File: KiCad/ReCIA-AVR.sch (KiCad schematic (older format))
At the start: 6 parts, among them U1 AVR128DA64-I_MR, U5 8520_DIP

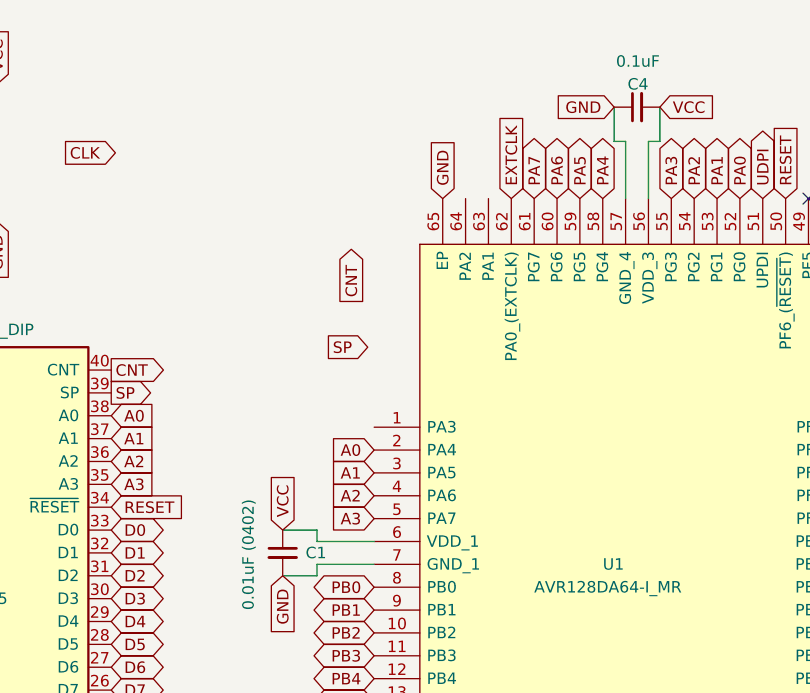
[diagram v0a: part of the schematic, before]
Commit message: Pin assignment of A0-A3, SP, CNT signals for the AVR-version and more routing done
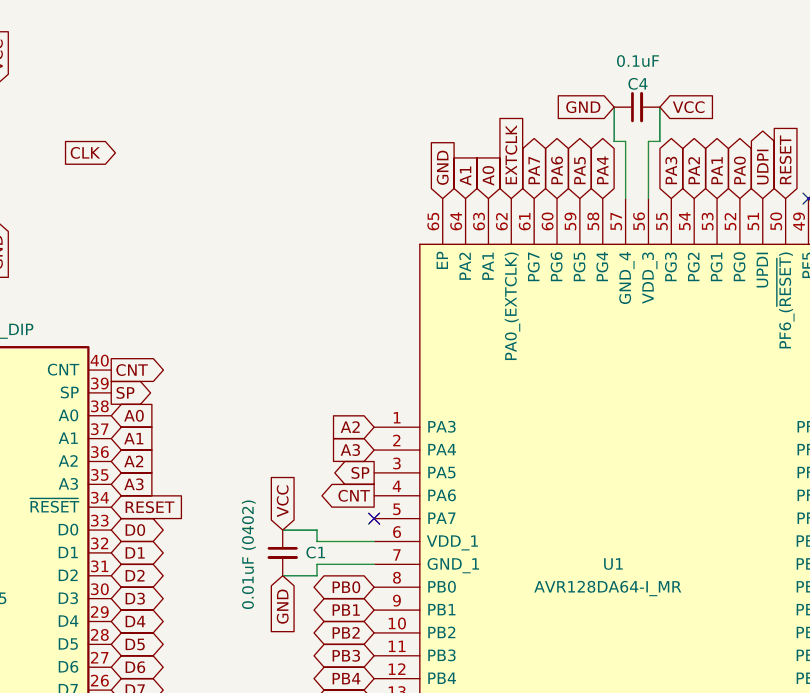
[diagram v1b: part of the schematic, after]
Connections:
- no-connect marks 13 -> 14
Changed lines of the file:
@@
 Text GLabel 5100 1650 1    50   BiDi ~ 0
 PA7
+Text GLabel 4900 1650 1    50   Input ~ 0
+A0
+Text GLabel 4800 1650 1    50   Input ~ 0
+A1
+Text GLabel 4400 2650 0    50   Input ~ 0
+A2
 Text GLabel 4400 2750 0    50   Input ~ 0
-A0
-Text GLabel 4400 2850 0    50   Input ~ 0
-A1
-Text GLabel 4400 2950 0    50   Input ~ 0
-A2
-Text GLabel 4400 3050 0    50   Input ~ 0
 A3
 Text GLabel 6100 1650 1    50   BiDi ~ 0
@@
 Text GLabel 5000 1650 1    50   Input ~ 0
 EXTCLK
-Text GLabel 4300 2100 1    50   Output ~ 0
+Text GLabel 4400 2950 0    50   Output ~ 0
 CNT
-Text GLabel 4200 2300 2    50   Output ~ 0
+Text GLabel 4400 2850 0    50   Output ~ 0
 SP
 NoConn ~ 6600 3150
@@
 Wire Wire Line
 	5150 5100 5150 5250
+NoConn ~ 4400 3050
 $EndSCHEMATC

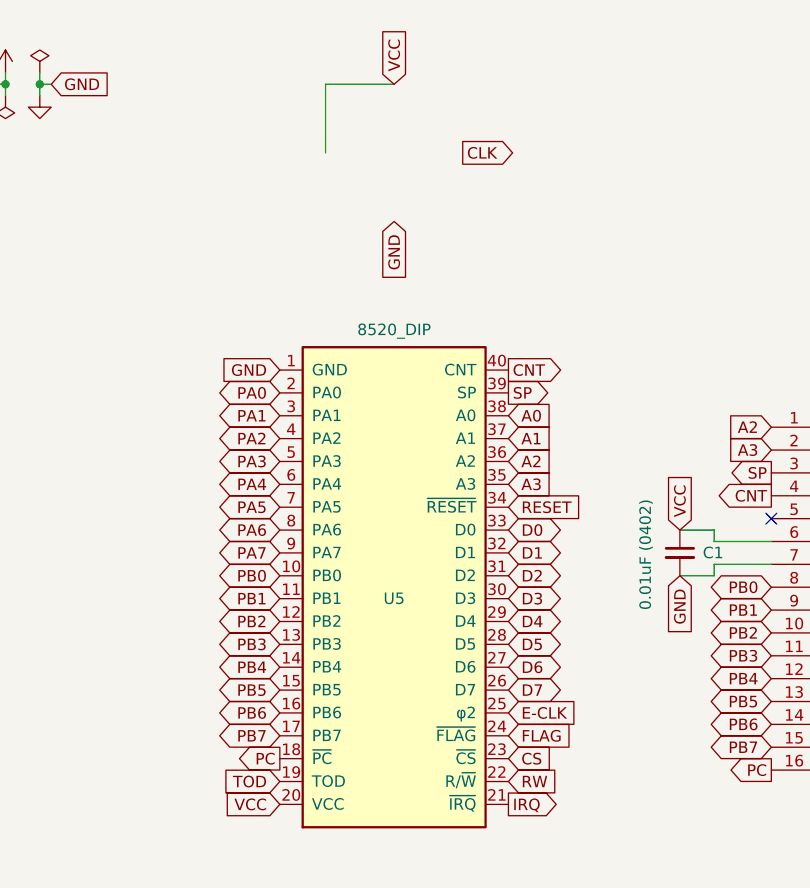
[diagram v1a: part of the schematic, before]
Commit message: Add a 74AHCT1G17 - Single Schmitt trigger buffer for the E-CLK on the AVR version
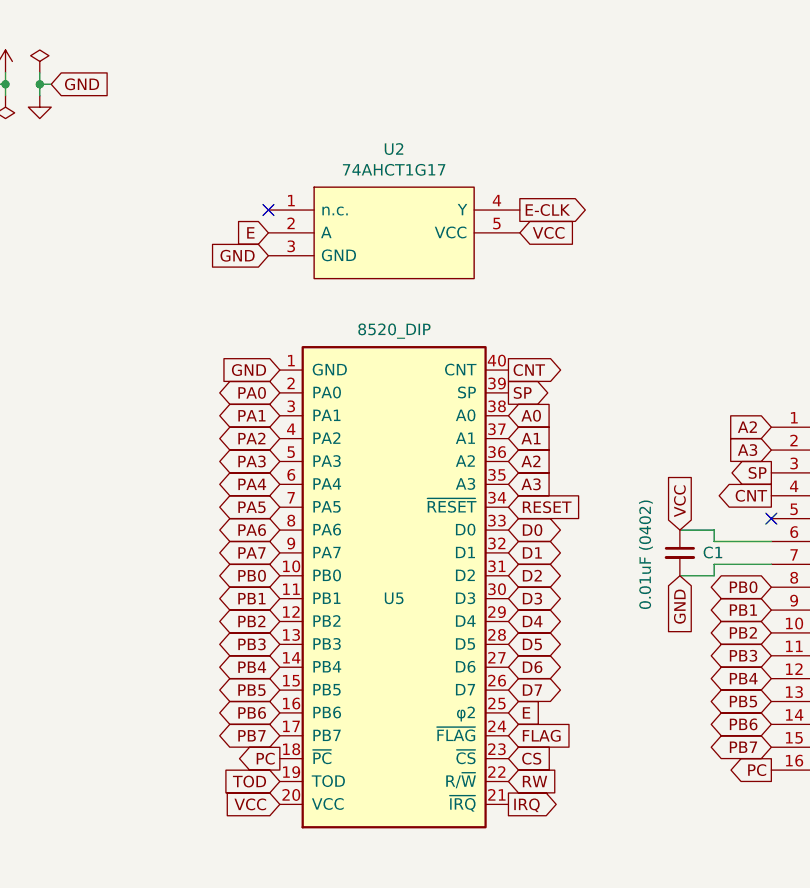
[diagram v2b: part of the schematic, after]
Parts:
- added U2: 74AHCT1G17, ReCIA:SOT95P275X110-5N, symbol ReCIA:74AHCT1G17
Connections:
- net labels added: E
- net labels removed: CLK
- wire segments 32 -> 30
- no-connect marks 14 -> 15
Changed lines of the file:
@@
 Text GLabel 3250 3800 2    50   BiDi ~ 0
 D7
-Text GLabel 3250 3900 2    50   Input ~ 0
+Text GLabel 3300 1700 2    50   Output ~ 0
 E-CLK
 Text GLabel 2250 4100 0    50   Output ~ 0
@@
 NoConn ~ 6600 2650
 NoConn ~ 6300 1650
-Text GLabel 2750 1750 3    50   Input ~ 0
-GND
-Text GLabel 2750 1150 1    50   Input ~ 0
-VCC
-Wire Wire Line
-	2450 1450 2450 1150
-Wire Wire Line
-	2450 1150 2750 1150
-Text GLabel 3050 1450 2    50   Output ~ 0
-CLK
 $Comp
 L Device:C_Small C1
@@
 	5150 5100 5150 5250
 NoConn ~ 4400 3050
+$Comp
+L ReCIA:74AHCT1G17 U2
+U 1 1 677A8B23
+P 2750 1800
+F 0 "U2" H 2750 2165 50  0000 C CNN
+F 1 "74AHCT1G17" H 2750 2074 50  0000 C CNN
+F 2 "ReCIA:SOT95P275X110-5N" H 3150 2000 50  0001 L CNN
+F 3 "https://assets.nexperia.com/documents/data-sheet/74AHC_AHCT1G17.pdf" H 3150 1900 50  0001 L CNN
+	1    2750 1800
+	1    0    0    -1
+$EndComp
+Text GLabel 2200 1900 0    50   Input ~ 0
+GND
+NoConn ~ 2200 1700
+Text GLabel 3300 1800 2    50   Input ~ 0
+VCC
+Text GLabel 3250 3900 2    50   Input ~ 0
+E
+Text GLabel 2200 1800 0    50   Input ~ 0
+E
 $EndSCHEMATC

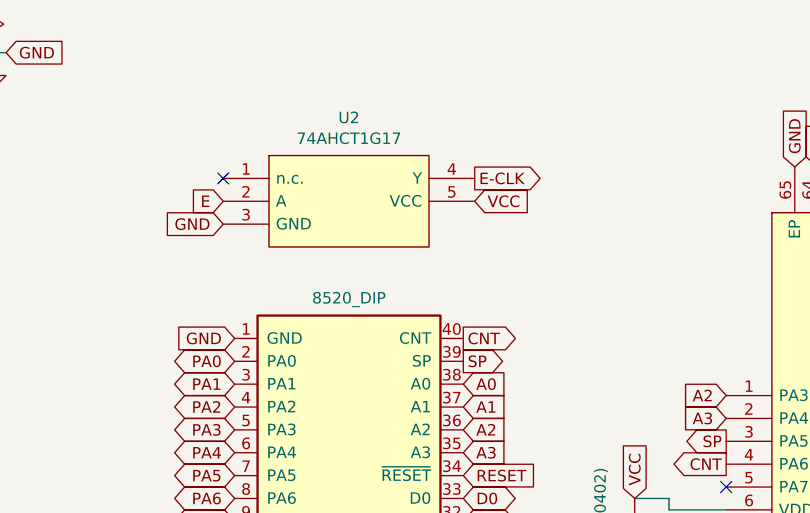
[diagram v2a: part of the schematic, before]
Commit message: Add decoupling cap for 74AHCT1G17 on the AVR version
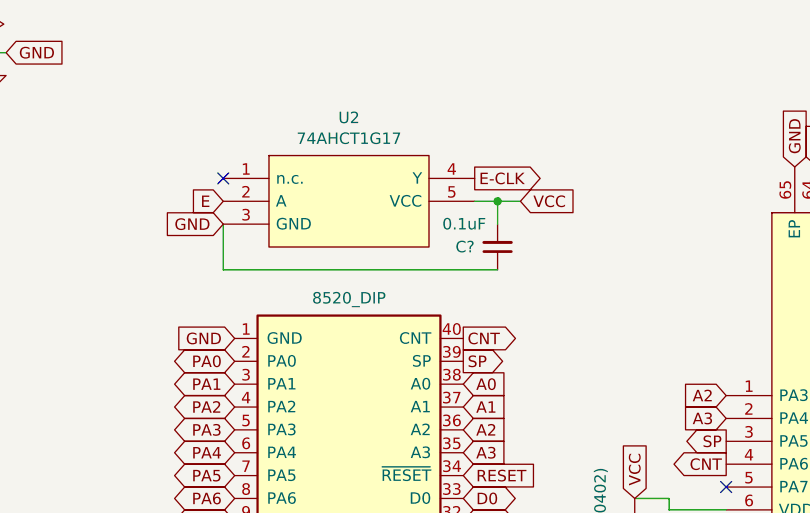
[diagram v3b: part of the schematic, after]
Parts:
- added C?: 0.1uF, Capacitor_SMD:C_0603_1608Metric_Pad1.08x0.95mm_HandSolder, symbol Device:C_Small
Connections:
- net GND: now also C?.1
- net VCC: now also C?.2
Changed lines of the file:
@@
 GND
 NoConn ~ 2200 1700
-Text GLabel 3300 1800 2    50   Input ~ 0
+Text GLabel 3500 1800 2    50   Input ~ 0
 VCC
 Text GLabel 3250 3900 2    50   Input ~ 0
@@
 Text GLabel 2200 1800 0    50   Input ~ 0
 E
+$Comp
+L Device:C_Small C?
+U 1 1 677B6FA1
+P 3400 2000
+F 0 "C?" H 3500 2000 50  0000 L CNN
+F 1 "0.1uF" H 3450 1900 50  0000 L CNN
+F 2 "Capacitor_SMD:C_0603_1608Metric_Pad1.08x0.95mm_HandSolder" H 3400 2000 50  0001 C CNN
+F 3 "~" H 3400 2000 50  0001 C CNN
+	1    3400 2000
+	-1   0    0    1
+$EndComp
+Wire Wire Line
+	3300 1800 3400 1800
+Wire Wire Line
+	3400 1900 3400 1800
+Connection ~ 3400 1800
+Wire Wire Line
+	3400 1800 3500 1800
+Wire Wire Line
+	3400 2100 2200 2100
+Wire Wire Line
+	2200 2100 2200 1900
 $EndSCHEMATC

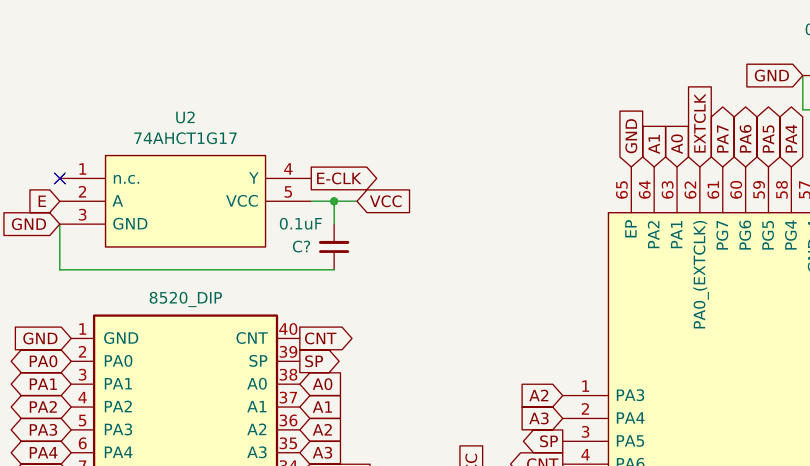
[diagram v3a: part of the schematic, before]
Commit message: Add a 33 Ohm damping resistor on the E-CLK buffer out line
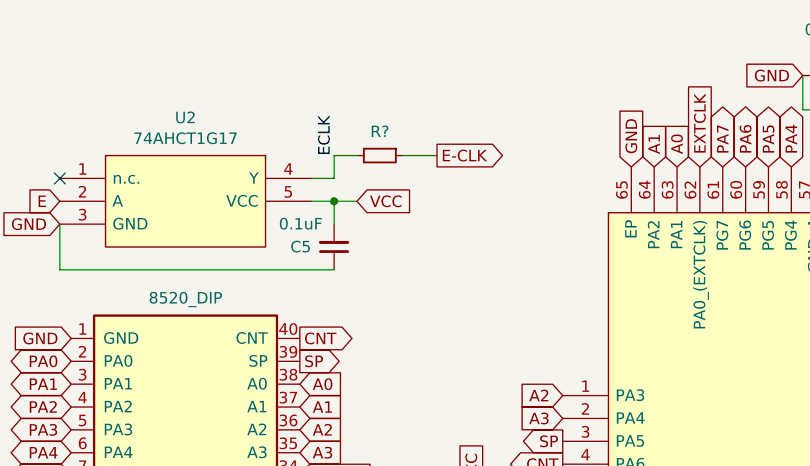
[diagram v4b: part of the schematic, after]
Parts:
- added R?: 33, Resistor_SMD:R_0603_1608Metric_Pad0.98x0.95mm_HandSolder, symbol Device:R_Small
- gave numbers to parts that had none: 1
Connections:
- net E-CLK: now also R?.1; no longer U2.4 (Y)
- new net ECLK: R?.2, U2.4 (Y)
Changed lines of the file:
@@
 Text GLabel 3250 3800 2    50   BiDi ~ 0
 D7
-Text GLabel 3300 1700 2    50   Output ~ 0
+Text GLabel 3850 1600 2    50   Output ~ 0
 E-CLK
 Text GLabel 2250 4100 0    50   Output ~ 0
@@
 E
 $Comp
-L Device:C_Small C?
+L Device:C_Small C5
 U 1 1 677B6FA1
 P 3400 2000
-F 0 "C?" H 3500 2000 50  0000 L CNN
+F 0 "C5" H 3500 2000 50  0000 L CNN
 F 1 "0.1uF" H 3450 1900 50  0000 L CNN
 F 2 "Capacitor_SMD:C_0603_1608Metric_Pad1.08x0.95mm_HandSolder" H 3400 2000 50  0001 C CNN
@@
 Wire Wire Line
 	2200 2100 2200 1900
+$Comp
+L Device:R_Small R?
+U 1 1 677C3D65
+P 3600 1600
+F 0 "R?" V 3496 1600 50  0000 C CNN
+F 1 "33" V 3495 1600 50  0001 C CNN
+F 2 "Resistor_SMD:R_0603_1608Metric_Pad0.98x0.95mm_HandSolder" H 3600 1600 50  0001 C CNN
+F 3 "~" H 3600 1600 50  0001 C CNN
+	1    3600 1600
+	0    1    1    0
+$EndComp
+Wire Wire Line
+	3300 1700 3400 1700
+Wire Wire Line
+	3400 1700 3400 1600
+Wire Wire Line
+	3400 1600 3500 1600
+Wire Wire Line
+	3700 1600 3850 1600
+Text Label 3400 1600 1    50   ~ 0
+ECLK
 $EndSCHEMATC

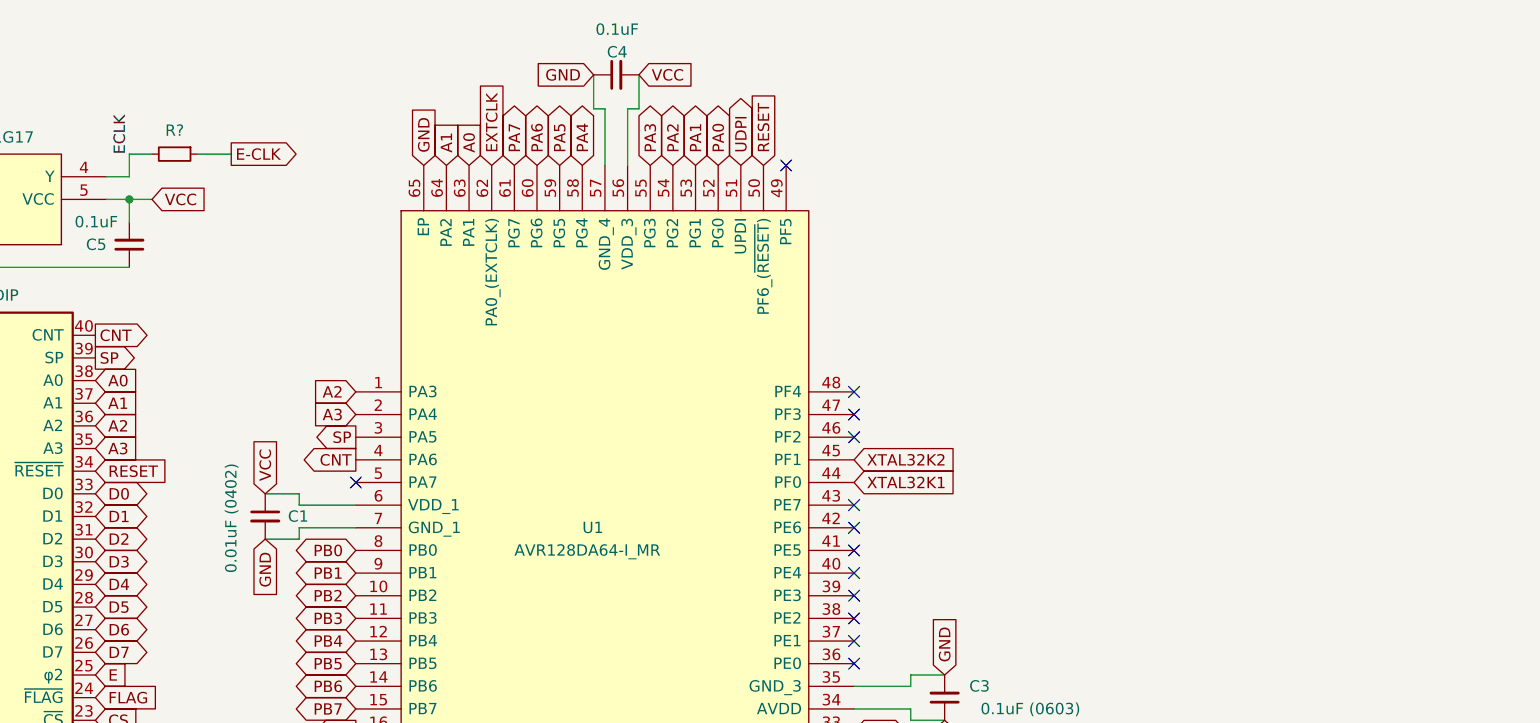
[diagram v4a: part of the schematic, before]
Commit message: Add TLC2932AIPWR to the AVR version
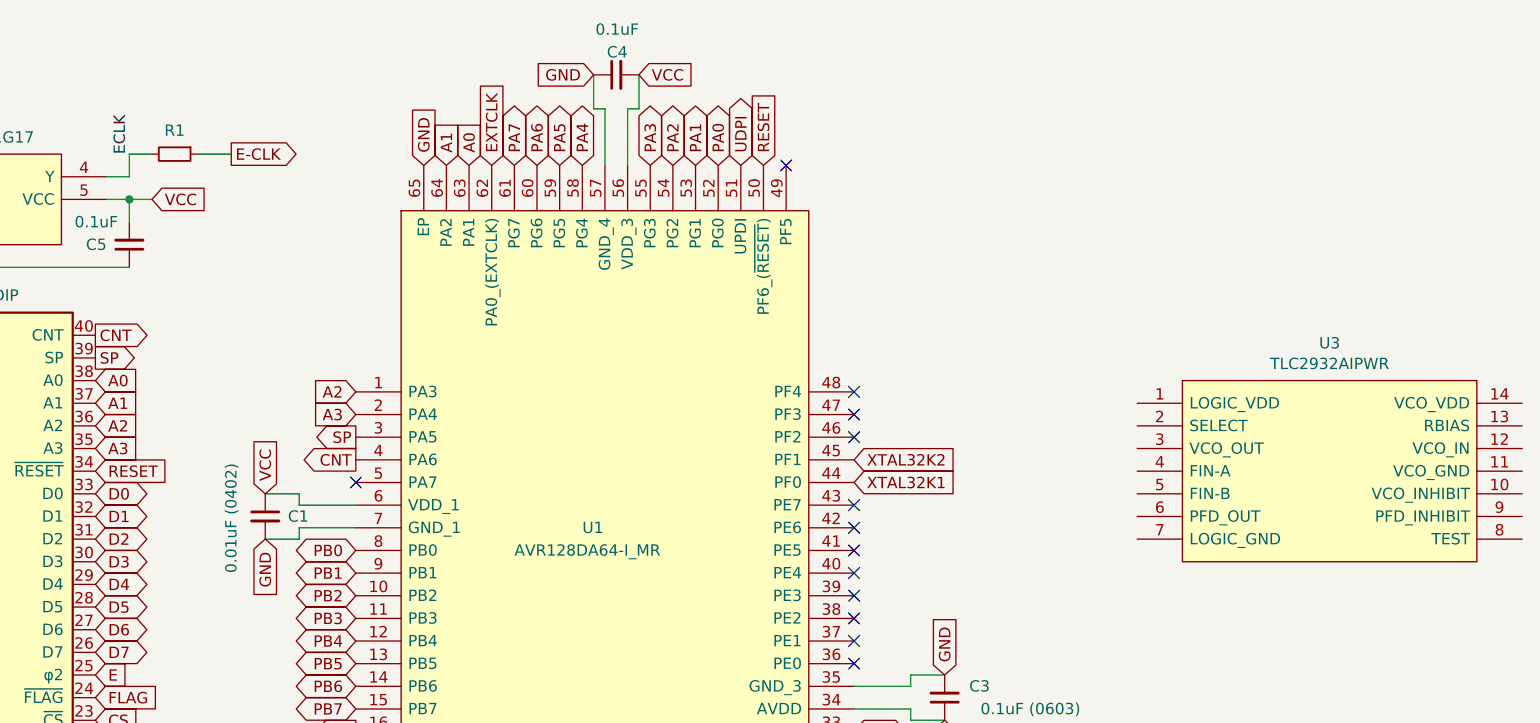
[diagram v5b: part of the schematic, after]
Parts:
- added U3: TLC2932AIPWR, Package_SO:TSSOP-14_4.4x5mm_P0.65mm, symbol ReCIA:TLC2932AIPWR
- gave numbers to parts that had none: 1
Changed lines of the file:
@@
 	2200 2100 2200 1900
 $Comp
-L Device:R_Small R?
+L Device:R_Small R1
 U 1 1 677C3D65
 P 3600 1600
-F 0 "R?" V 3496 1600 50  0000 C CNN
+F 0 "R1" V 3496 1600 50  0000 C CNN
 F 1 "33" V 3495 1600 50  0001 C CNN
 F 2 "Resistor_SMD:R_0603_1608Metric_Pad0.98x0.95mm_HandSolder" H 3600 1600 50  0001 C CNN
@@
 Text Label 3400 1600 1    50   ~ 0
 ECLK
+$Comp
+L ReCIA:TLC2932AIPWR U3
+U 1 1 677DB716
+P 8650 2950
+F 0 "U3" H 8700 3465 50  0000 C CNN
+F 1 "TLC2932AIPWR" H 8700 3374 50  0000 C CNN
+F 2 "Package_SO:TSSOP-14_4.4x5mm_P0.65mm" H 9400 3300 50  0001 L CNN
+F 3 "http://www.ti.com/lit/gpn/TLC2932A" H 9400 3200 50  0001 L CNN
+	1    8650 2950
+	1    0    0    -1
+$EndComp
 $EndSCHEMATC

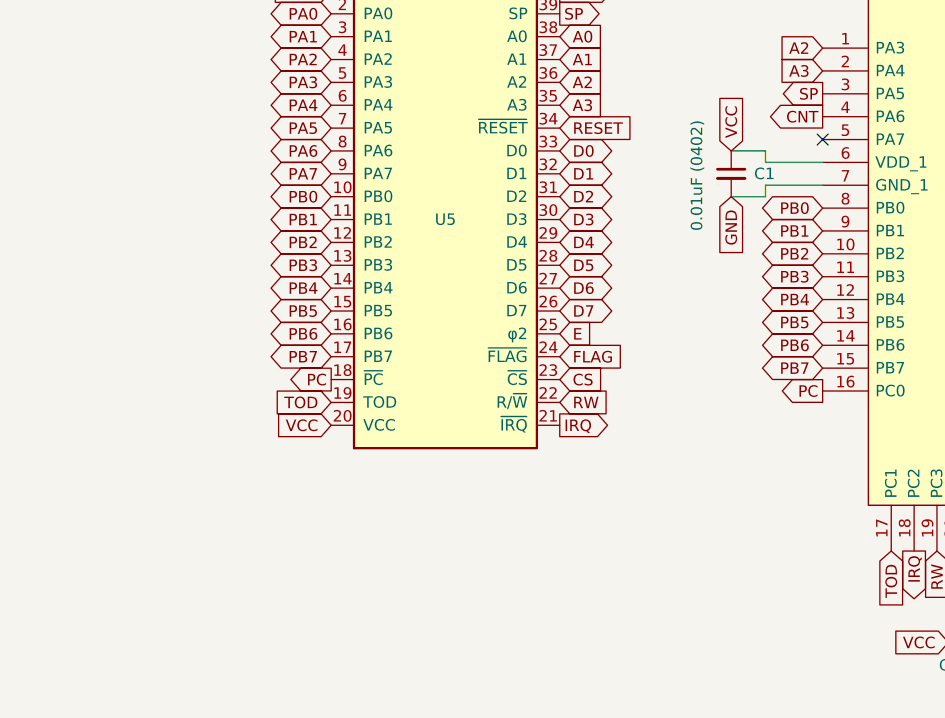
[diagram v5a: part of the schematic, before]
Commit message: Add 10uF 1206 capacitor on VCC input for the AVR version
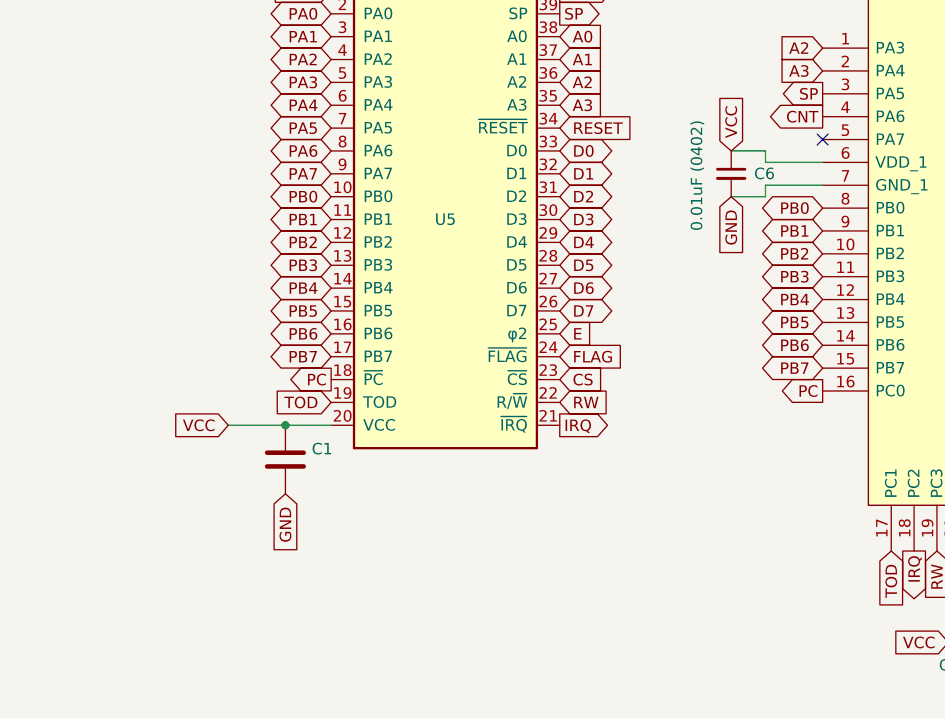
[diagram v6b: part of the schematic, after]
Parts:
- added C1: C, Capacitor_SMD:C_1206_3216Metric_Pad1.33x1.80mm_HandSolder, symbol Device:C
- renumbered C1 to C6
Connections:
- net GND: now also C1.2
- net VCC: now also C1.1
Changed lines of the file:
@@
 Wire Wire Line
 	1050 1150 1050 1200
-Text GLabel 2250 4300 0    50   Input ~ 0
+Text GLabel 1800 4300 0    50   Input ~ 0
 VCC
 $Comp
@@
 NoConn ~ 6300 1650
 $Comp
-L Device:C_Small C1
+L Device:C_Small C6
 U 1 1 66CAF364
 P 4000 3200
-F 0 "C1" H 4100 3200 50  0000 L CNN
+F 0 "C6" H 4100 3200 50  0000 L CNN
 F 1 "0.01uF (0402)" V 3850 2950 50  0000 L CNN
 F 2 "Capacitor_SMD:C_0402_1005Metric" H 4000 3200 50  0001 C CNN
@@
 	1    0    0    -1
 $EndComp
+$Comp
+L Device:C C1
+U 1 1 677E2BF6
+P 2050 4450
+F 0 "C1" H 2165 4496 50  0000 L CNN
+F 1 "C" H 2165 4405 50  0001 L CNN
+F 2 "Capacitor_SMD:C_1206_3216Metric_Pad1.33x1.80mm_HandSolder" H 2088 4300 50  0001 C CNN
+F 3 "~" H 2050 4450 50  0001 C CNN
+	1    2050 4450
+	1    0    0    -1
+$EndComp
+Wire Wire Line
+	1800 4300 2050 4300
+Connection ~ 2050 4300
+Wire Wire Line
+	2050 4300 2250 4300
+Text GLabel 2050 4600 3    50   Input ~ 0
+GND
 $EndSCHEMATC
